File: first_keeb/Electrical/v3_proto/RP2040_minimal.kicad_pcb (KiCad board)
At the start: 2 copper layers, 80 x 60 mm, 68 parts, among them J1 Conn_01x05_Socket, J2 Conn_01x01_Socket, P1 USB4105-GF-A, Q1 BSS138, SW1 SW_Push, SW2 SW_Push, U1 NCP1117-3.3_SOT223, U2 LM4040DBZ-3, U3 PRTR5V0U2X, U4 W25Q32JVSS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

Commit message: finishes circular pcb
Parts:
- removed J1: Conn_01x05_Socket, Connector_PinSocket_2.54mm:PinSocket_1x05_P2.54mm_Vertical
- removed J2: Conn_01x01_Socket, Connector_PinSocket_2.54mm:PinSocket_1x01_P2.54mm_Vertical
- removed the REF** at (65.5, 74.8)
- removed the REF** at (65.5, 124.8)
- removed the REF** at (134.5, 74.8)
- removed the REF** at (134.5, 124.8)
- added C29: 100n, Capacitor_SMD:C_0402_1005Metric, F.Cu at (87.5, 85.6)
- added D8: WS2812B-2020, LED_SMD:LED_WS2812B-2020_PLCC4_2.0x2.0mm, F.Cu at (84.7, 86.1)
- added REF**: MountingHole_3.2mm_M3, MountingHole:MountingHole_3.2mm_M3, F.Cu at (100.0, 132.0)
- added REF**: MountingHole_3.2mm_M3, MountingHole:MountingHole_3.2mm_M3, F.Cu at (72.0, 84.0)
- added REF**: MountingHole_3.2mm_M3, MountingHole:MountingHole_3.2mm_M3, F.Cu at (128.0, 84.0)
- C22, C24, C26, C28: value 1u -> 100n
- C23, C25, C27: value 1u -> 100n; moved to F.Cu
- D1, D3: value WS2812B -> WS2812B-2020; footprint Keebio-Parts:WS2812B -> LED_SMD:LED_WS2812B-2020_PLCC4_2.0x2.0mm
- D2, D4: value WS2812B -> WS2812B-2020; footprint Keebio-Parts:WS2812B -> LED_SMD:LED_WS2812B-2020_PLCC4_2.0x2.0mm; moved to F.Cu
- D5, D7: value SK6812MINI -> WS2812B-2020; footprint Keebio-Parts:SK6812-MINI-E -> LED_SMD:LED_WS2812B-2020_PLCC4_2.0x2.0mm
- D6: value SK6812MINI -> WS2812B-2020; footprint Keebio-Parts:SK6812-MINI-E -> LED_SMD:LED_WS2812B-2020_PLCC4_2.0x2.0mm; moved to F.Cu
- moved S1 173.4 mm to (119.5, 100.0), turned to 0 degrees
- moved C19 172.2 mm to (116.9, 101.5), turned to 90 degrees
- moved D1 155.8 mm to (121.1, 112.8), turned to 0 degrees
- moved D2 155.3 mm to (120.2, 114.5), turned to 0 degrees
- moved C22 153.7 mm to (123.8, 113.4)
- moved C23 153.1 mm to (122.9, 114.0)
- moved R10 147.6 mm to (129.6, 91.3)
- moved Q1 147.4 mm to (126.8, 90.9), turned to -90 degrees
- moved R9 146.5 mm to (123.6, 91.9), turned to 0 degrees
- moved C20 140.2 mm to (97.2, 98.6)
- moved S2 140.2 mm to (100.0, 100.0)
- moved C21 134.6 mm to (79.5, 96.7)
- moved S3 134.6 mm to (80.5, 100.0)
- moved U2 133.9 mm to (95.0, 90.7)
- moved R1 133.9 mm to (91.3, 91.5)
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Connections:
- D1 pad 1: +5V -> Net-(D1-DOUT)
- D1 pad 2: Net-(D1-DOUT) -> GND
- D1 pad 3: GND -> LED_D_5V
- D1 pad 4: LED_D_5V -> +5V
- D2 pad 1: +5V -> Net-(D2-DOUT)
- D2 pad 2: Net-(D2-DOUT) -> GND
- D2 pad 3: GND -> Net-(D1-DOUT)
- D2 pad 4: Net-(D1-DOUT) -> +5V
- D3 pad 1: +5V -> Net-(D3-DOUT)
- D3 pad 2: Net-(D3-DOUT) -> GND
- D3 pad 3: GND -> Net-(D2-DOUT)
- D3 pad 4: Net-(D2-DOUT) -> +5V
- D4 pad 1: +5V -> Net-(D4-DOUT)
- D4 pad 2: Net-(D4-DOUT) -> GND
- D4 pad 3: GND -> Net-(D3-DOUT)
- D4 pad 4: Net-(D3-DOUT) -> +5V
- D7 pad 1: unconnected-(D7-DOUT-Pad1) -> Net-(D7-DOUT)
- Q1 pad 2: GPIO12 -> /GPIO17
- R9 pad 2: GPIO12 -> /GPIO17
- U3 pad 2: /USB_D+ -> /USB_D-
- U3 pad 3: /USB_D- -> /USB_D+
- U5 pad 13: BUTT0 -> /GPIO10
- U5 pad 14: BUTT1 -> /GPIO11
- U5 pad 29: /GPIO18 -> BUTT0
- U5 pad 30: /GPIO19 -> BUTT1
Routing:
- net +5V: track 32.3 -> 185.0 mm, vias 0 -> 4
- net BUTT1: track 0.00 -> 83.5 mm, vias 0 -> 2
- net BUTT0: track 0.00 -> 64.0 mm, vias 0 -> 2
- net Net-(D6-DOUT): track 0.73 -> 47.6 mm, vias 0 -> 1
- net Net-(D4-DOUT): track 0.81 -> 31.6 mm, vias 0 -> 1
- net Net-(D2-DOUT): track 1.47 -> 27.4 mm, vias 0 -> 1
- net LED_D_5V: track 7.77 -> 29.6 mm
- net RP_ADC2: track 8.49 -> 30.1 mm
- net /GPIO17: track 0.00 -> 20.2 mm
- net /QSPI_SD1: track 3.39 -> 19.2 mm
- net /USB_D+: track 10.6 -> 25.9 mm
- net /USB_D-: track 10.4 -> 25.1 mm
- net /QSPI_SS: track 6.62 -> 21.0 mm
- net /QSPI_SD2: track 4.05 -> 16.1 mm
- net RP_ADC0: track 8.63 -> 18.0 mm
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- removed copper zone on B.Cu, net +5V
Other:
- board size 80 x 60 mm -> 76 x 76 mm

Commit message: finishes pcb even more
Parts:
- moved P1 2.00 mm to (100.0, 64.0)
- moved R2 2.00 mm to (98.1, 69.9)
- moved R3 2.00 mm to (101.7, 69.9)
- moved REF** 1.00 mm to (100.0, 133.0)
- moved REF** 1.00 mm to (71.0, 84.0)
- moved REF** 1.00 mm to (129.0, 84.0)
- moved C24 0.50 mm to (102.7, 124.8)
- moved C25 0.50 mm to (102.5, 124.2)
- moved D3 0.50 mm to (100.1, 124.2)
- moved D4 0.50 mm to (100.0, 124.7)
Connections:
- net /GPIO17 renamed GPIO17
- net BUTT0 renamed GPIO18
- net BUTT1 renamed GPIO19
- net GPIO12 renamed /GPIO12
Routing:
- net +5V: track 185.0 -> 187.5 mm
- net /USB_D-: track 25.1 -> 27.5 mm
- net /USB_D+: track 25.9 -> 28.1 mm
- net VBUS: track 19.7 -> 21.4 mm
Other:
- board size 76 x 76 mm -> 80 x 80 mm

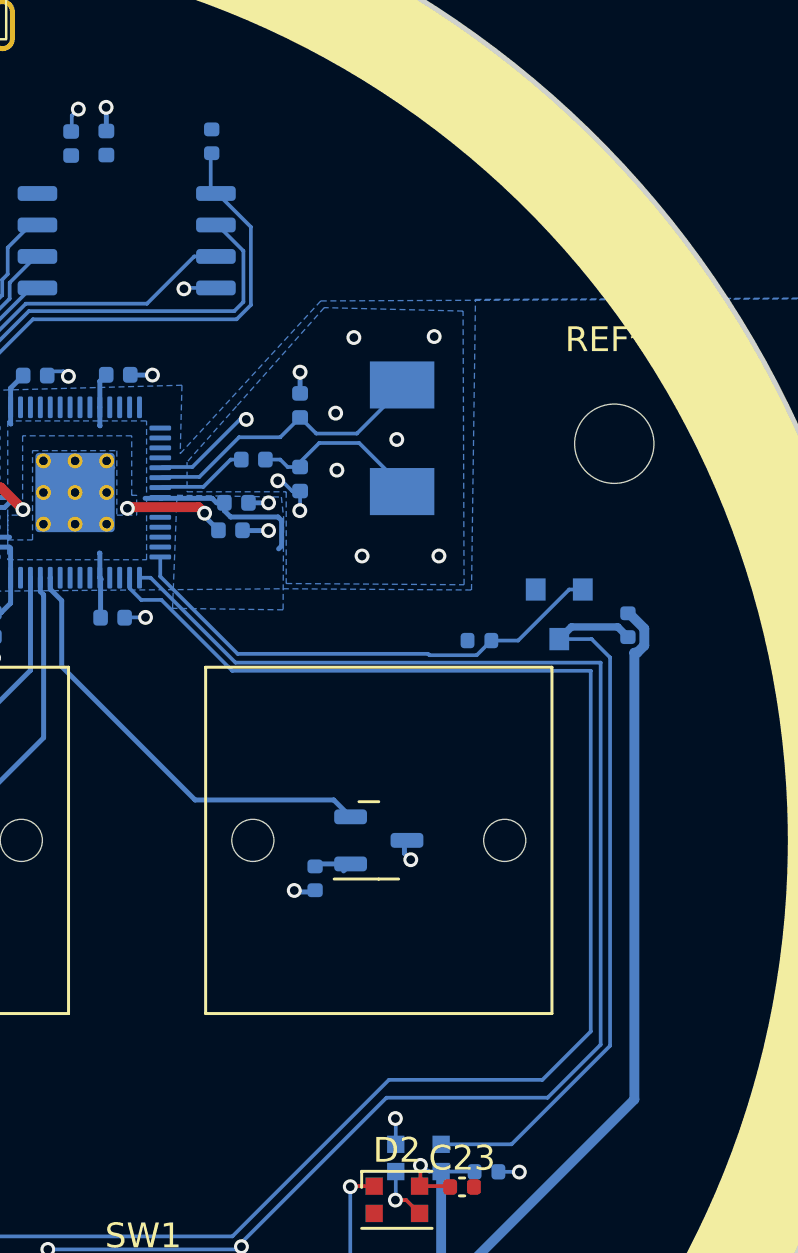
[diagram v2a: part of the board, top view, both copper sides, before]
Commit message: ads bootsel button and changes pcb to 80mm diameter
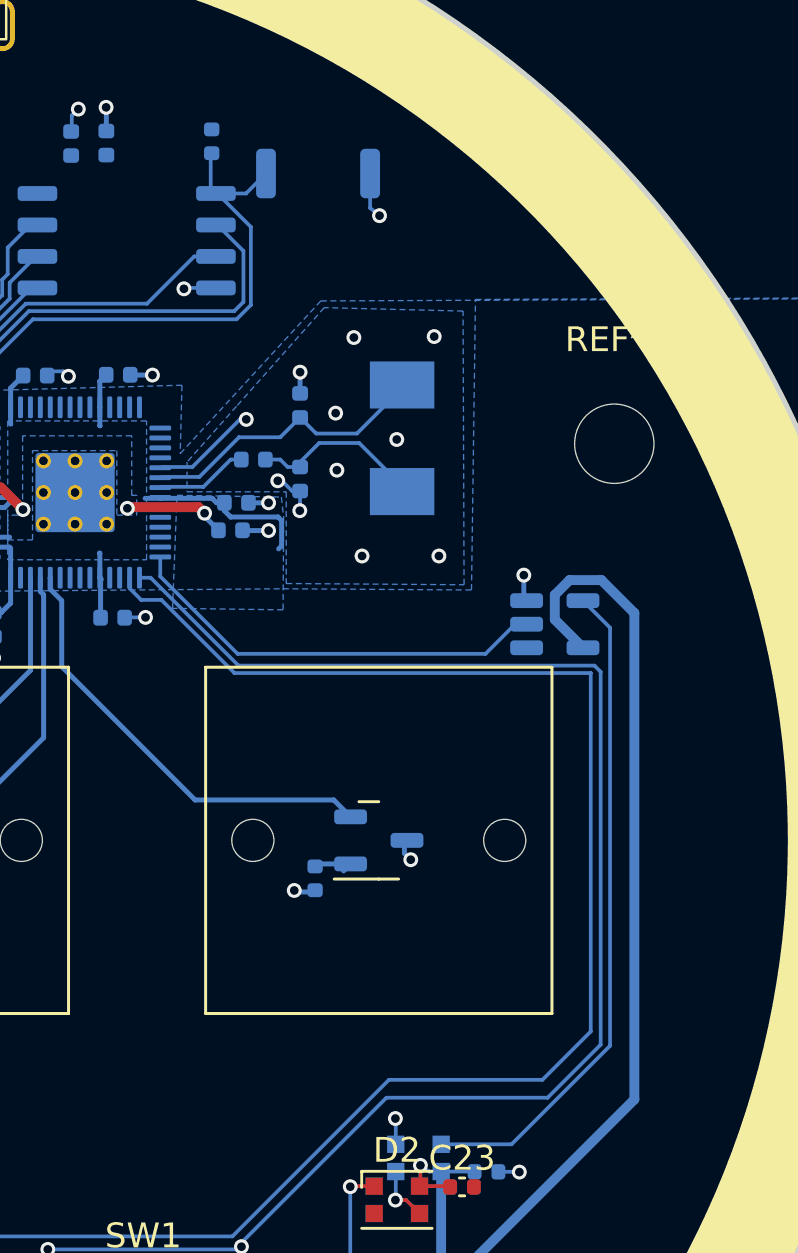
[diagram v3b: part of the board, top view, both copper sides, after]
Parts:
- removed R10, R9: 10k, Capacitor_SMD:C_0402_1005Metric
- added SW3: SKRKAGE020, Button_Switch_SMD:SW_Push_SPST_NO_Alps_SKRK, B.Cu at (117.0, 73.1)
- Q1: value BSS138 -> SN74LV1T34DBV; footprint Keebio-Parts:SOT-23 -> Package_TO_SOT_SMD:SOT-23-5
- moved Q1 0.44 mm to (126.6, 91.3), turned to 0 degrees
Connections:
- Q1 pad 1: +3V3 -> unconnected-(Q1-NC-Pad1)
- Q1 pad 3: LED_D_5V -> GND
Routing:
- net +5V: track 187.5 -> 193.6 mm
- net GND: track 43.2 -> 46.4 mm, vias 49 -> 51
- net GPIO17: track 20.2 -> 17.4 mm
- net LED_D_5V: track 29.6 -> 26.9 mm
- net /QSPI_SS: track 21.0 -> 23.4 mm

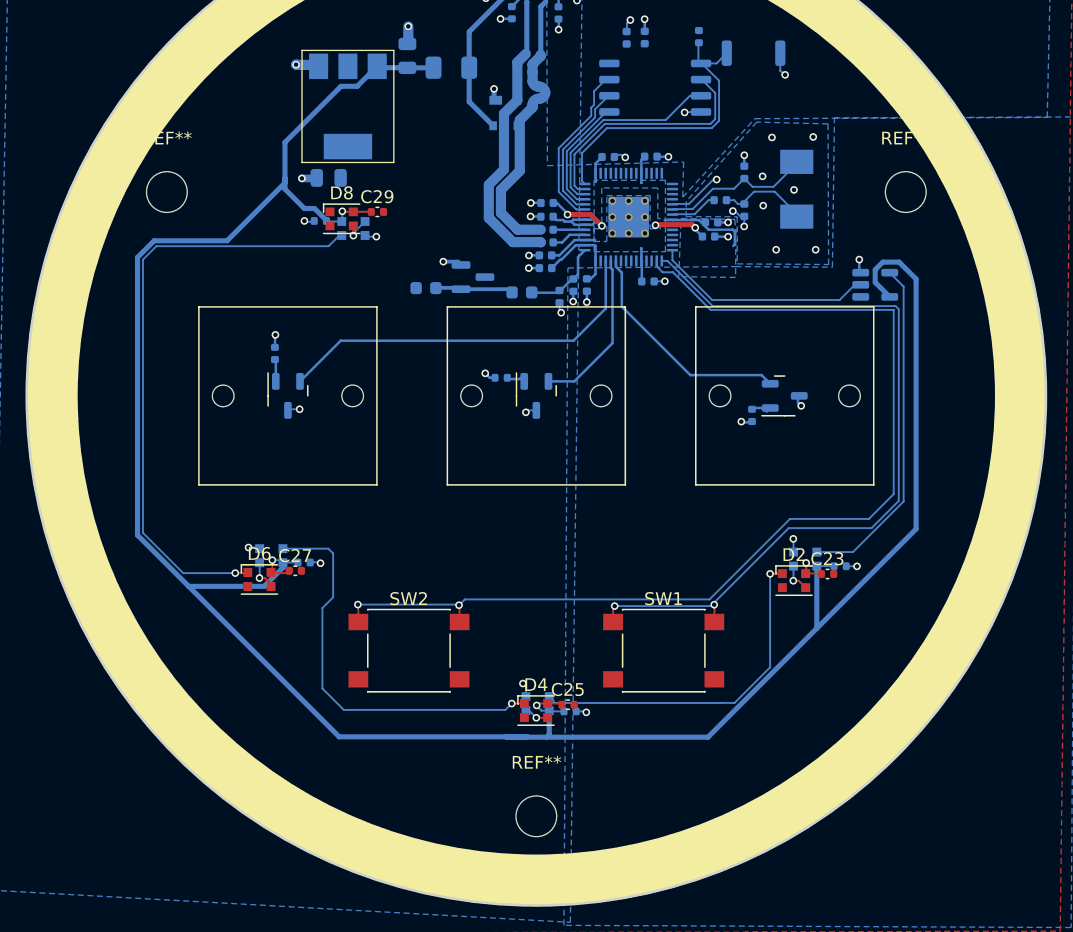
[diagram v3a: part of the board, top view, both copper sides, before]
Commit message: ads threaded mounting hole
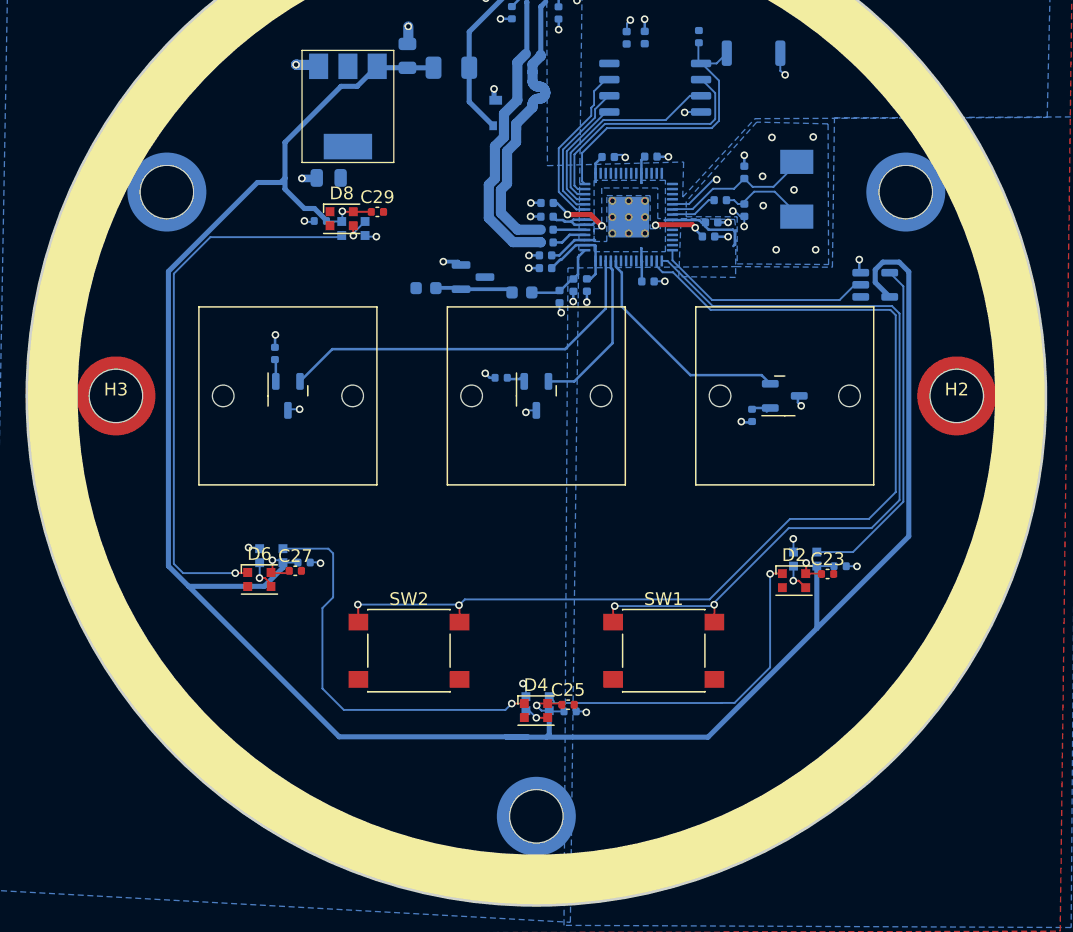
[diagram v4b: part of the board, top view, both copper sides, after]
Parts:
- removed the REF** at (100.0, 133.0)
- removed the REF** at (71.0, 84.0)
- removed the REF** at (129.0, 84.0)
- added H1: 4881_M3_Threaded_Insert, MountingHole:4881_M3_Threaded_Insert, B.Cu at (129.0, 84.0)
- added H2: 4881_M3_Threaded_Insert, MountingHole:4881_M3_Threaded_Insert, F.Cu at (133.0, 100.0)
- added H3: 4881_M3_Threaded_Insert, MountingHole:4881_M3_Threaded_Insert, F.Cu at (67.0, 100.0)
- added H4: 4881_M3_Threaded_Insert, MountingHole:4881_M3_Threaded_Insert, B.Cu at (71.0, 84.0)
- added H5: 4881_M3_Threaded_Insert, MountingHole:4881_M3_Threaded_Insert, B.Cu at (100.0, 133.0)
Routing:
- net +5V: track 193.6 -> 188.8 mm
- net Net-(D6-DOUT): track 47.6 -> 43.5 mm

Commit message: ordered pcb assembly
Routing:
- net Net-(D6-DOUT): track 43.5 -> 42.7 mm
